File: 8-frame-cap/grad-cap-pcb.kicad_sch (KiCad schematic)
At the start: 15 parts, among them J1 B02B-XASK-1LFSN, SW1 CUS-13TB, U1 MC74HC73ADR2G, U2 SN74HCS238DYYR, U3 ICM7555xB

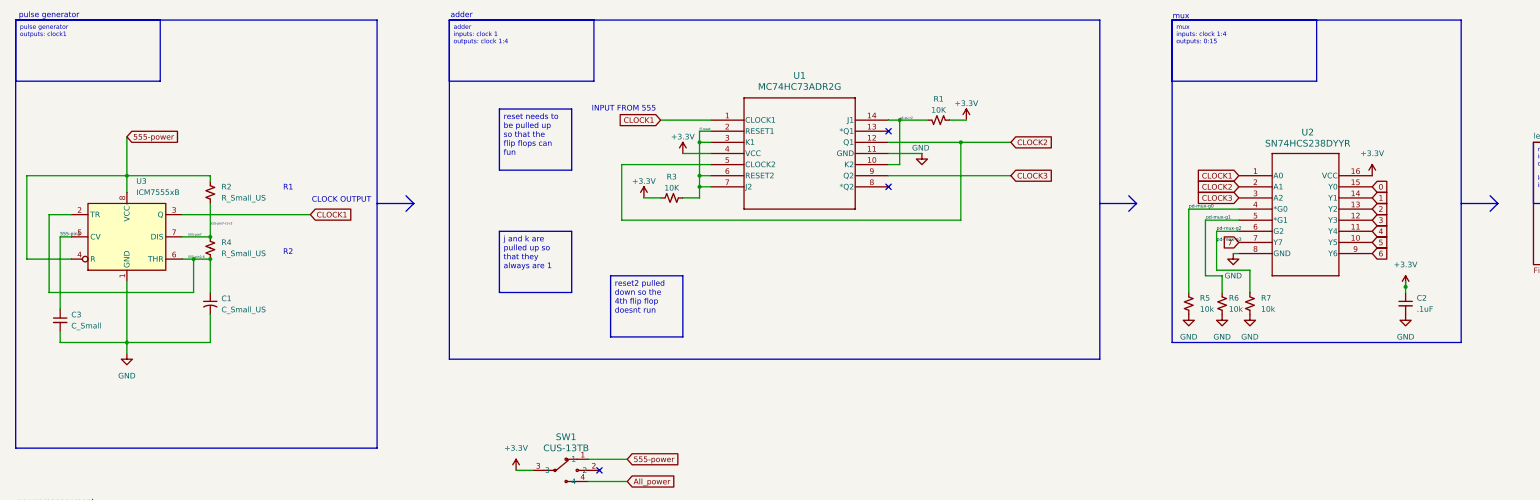
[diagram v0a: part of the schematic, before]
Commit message: routed traces, reorganized, renamed
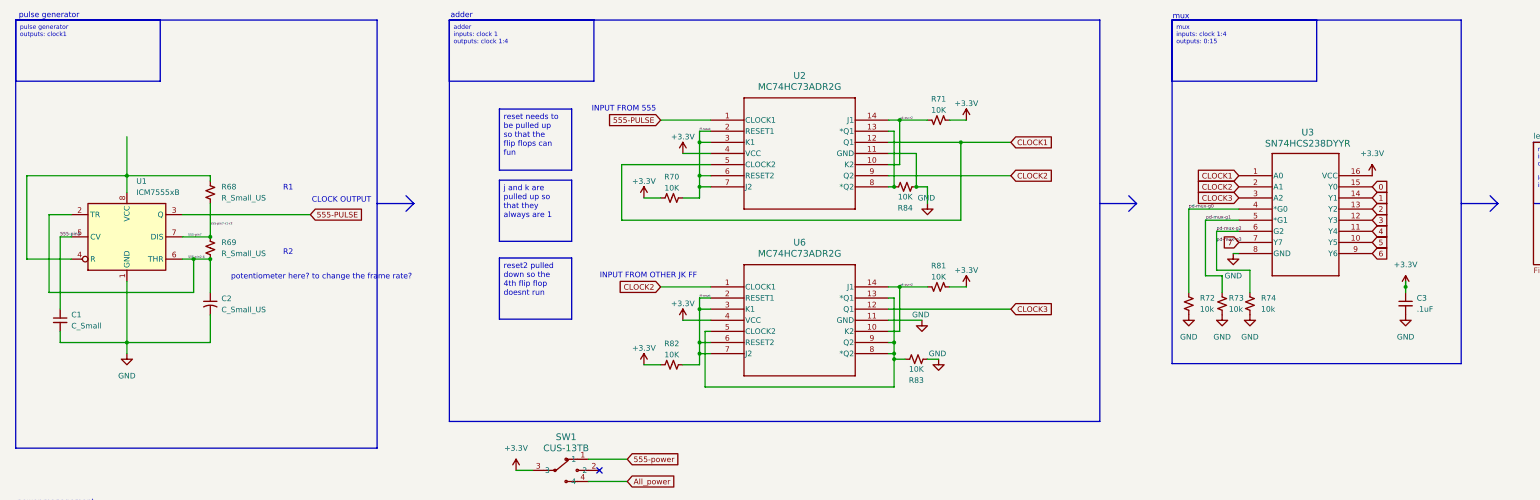
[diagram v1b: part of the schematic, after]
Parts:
- added R81, R82, R83, R84: 10K, Capacitor_SMD:C_0402_1005Metric_Pad0.74x0.62mm_HandSolder, symbol Device:R_Small_US
- added U6: MC74HC73ADR2G, GRAD-CAP:MC74HC73ADR2G_JK-FLIPFLOP, symbol MC74HC73ADR2G_JK-FLIPFLOP:MC74HC73ADR2G
- C1: renamed from C3; footprint Capacitor_SMD:C_0805_2012Metric_Pad1.18x1.45mm_HandSolder -> Capacitor_SMD:C_0603_1608Metric_Pad1.08x0.95mm_HandSolder
- C2: renamed from C1; footprint Capacitor_SMD:C_0805_2012Metric_Pad1.18x1.45mm_HandSolder -> Capacitor_SMD:C_0603_1608Metric_Pad1.08x0.95mm_HandSolder
- C3: renamed from C2; footprint Capacitor_SMD:C_0805_2012Metric_Pad1.18x1.45mm_HandSolder -> Capacitor_SMD:C_0603_1608Metric_Pad1.08x0.95mm_HandSolder
- R68: renamed from R2; footprint Resistor_SMD:R_0805_2012Metric_Pad1.20x1.40mm_HandSolder -> Resistor_SMD:R_0603_1608Metric_Pad0.98x0.95mm_HandSolder
- R69: renamed from R4; footprint Resistor_SMD:R_0805_2012Metric_Pad1.20x1.40mm_HandSolder -> Resistor_SMD:R_0603_1608Metric_Pad0.98x0.95mm_HandSolder
- R70: renamed from R3; footprint Resistor_SMD:R_0805_2012Metric_Pad1.20x1.40mm_HandSolder -> Capacitor_SMD:C_0402_1005Metric_Pad0.74x0.62mm_HandSolder
- R71: renamed from R1; footprint Resistor_SMD:R_0805_2012Metric_Pad1.20x1.40mm_HandSolder -> Capacitor_SMD:C_0402_1005Metric_Pad0.74x0.62mm_HandSolder
- R72: renamed from R5; footprint Capacitor_SMD:C_0805_2012Metric_Pad1.18x1.45mm_HandSolder -> Capacitor_SMD:C_0402_1005Metric_Pad0.74x0.62mm_HandSolder
- R73: renamed from R6; footprint Capacitor_SMD:C_0805_2012Metric_Pad1.18x1.45mm_HandSolder -> Capacitor_SMD:C_0402_1005Metric_Pad0.74x0.62mm_HandSolder
- R74: renamed from R7; footprint Capacitor_SMD:C_0805_2012Metric_Pad1.18x1.45mm_HandSolder -> Capacitor_SMD:C_0402_1005Metric_Pad0.74x0.62mm_HandSolder
- SW1: now left out of the parts list
- renumbered U3 to U1, U1 to U2, U2 to U3
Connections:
- net +3.3V: now also R81.1, R82.1, U6.4 (VCC)
- net 555-power: no longer R68.1, U1.4 (R), U1.8 (VCC)
- net CLOCK1: now also U2.12 (Q1), U2.5 (CLOCK2); no longer U1.3 (Q), U2.1 (CLOCK1)
- net CLOCK2: now also U2.9 (Q2), U6.1 (CLOCK1); no longer U2.12 (Q1), U2.5 (CLOCK2)
- net CLOCK3: now also U6.12 (Q1); no longer U2.9 (Q2)
- net GND: now also R83.1, R84.1, U6.11 (GND)
- net ff-reset: now also R82.2, U6.2 (RESET1), U6.3 (K1), U6.6 (RESET2), U6.7 (J2)
- net u4-pu-r2: now also R81.2, U6.10 (K2), U6.14 (J1)
- net at U2.13 (*Q1): now also U2.8 (*Q2), R84.2
- new net: R83.2, U6.13 (*Q1), U6.5 (CLOCK2), U6.8 (*Q2), U6.9 (Q2)
- new net: R68.1, U1.4 (R), U1.8 (VCC)
- new net 555-PULSE: U1.3 (Q), U2.1 (CLOCK1)
- no-connect marks 3 -> 1
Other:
- note added: "INPUT FROM OTHER JK FF"
- note added: "potentiometer here? to change the frame rate?"

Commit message: updated pcb
error checking
90* angles removal
schematic relinking
reorganizing schematic
fixed footprints for PHPT6 (mosfets, they didnt like the pads and the body being "different" pours or something)
silkscreen reorg
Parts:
- removed C2: C_Small_US, Capacitor_SMD:C_0603_1608Metric_Pad1.08x0.95mm_HandSolder, symbol Device:C_Small_US
- removed U1: ICM7555xB, Package_SO:SOIC-8_3.9x4.9mm_P1.27mm, symbol Timer:ICM7555xB
- added C2, C4: .1uF, Capacitor_SMD:C_0603_1608Metric_Pad1.08x0.95mm_HandSolder, symbol Device:C_Small
- added R75, R76, R77: 10k, Resistor_SMD:R_0603_1608Metric_Pad0.98x0.95mm_HandSolder, symbol Device:R_Small_US
- added T1, T2, T3, T4, T5, T6, T7: PHPT610035PKX, GRAD-CAP:PHPT610035PKX_TRANS-2PNP-100V-3A, symbol PHPT610035PKX_TRANS-2PNP-100V-3A:PHPT610035PKX
- added U1: MIC1557YM5-TR, SOT-23-5_M5_MCH, symbol MIC1557:MIC1557YM5-TR
- added U4, U5: SN74AHCT32DBR, GRAD-CAP:SN74AHCT32DBR_2-INPUT-QUAD-OR, symbol SN74AHCT32DBR_2-INPUT-QUAD-OR:SN74AHCT32DBR
- C1: value C_Small -> .68uF
- R68: value R_Small_US -> 1M
- R69: value R_Small_US -> 270k
- R70, R71, R72, R73, R74, R81, R82, R83, R84: footprint Capacitor_SMD:C_0402_1005Metric_Pad0.74x0.62mm_HandSolder -> Resistor_SMD:R_0603_1608Metric_Pad0.98x0.95mm_HandSolder
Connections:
- net 555-pin2-6 is gone; now on net 557-PULSE: R69.2
- net +3.3V: now also R68.1, C2.1, C4.1, T1.1 (EMITTER), T1.3 (EMITTER), T2.1 (EMITTER), T2.3 (EMITTER), T3.1 (EMITTER), T3.3 (EMITTER), T4.1 (EMITTER), T4.3 (EMITTER), T5.1 (EMITTER), T5.3 (EMITTER), T6.1 (EMITTER), T6.3 (EMITTER), T7.1 (EMITTER), T7.3 (EMITTER), U1.4 (VS), U4.14 (VCC), U5.14 (VCC)
- net 0: now also U5.1 (1A), U5.12 (4A)
- net 1: now also U5.2 (1B), U5.4 (2A)
- net 2: now also U5.5 (2B)
- net 3: now also U4.9 (3A)
- net 4: now also U4.10 (3B), U4.2 (1B)
- net 5: now also U4.1 (1A), U4.13 (4B)
- net 6: now also U4.12 (4A), U5.9 (3A)
- net 7: now also U5.10 (3B), U5.13 (4B)
- net GND: now also C2.2, C4.2, R75.2, R76.2, R77.2, U1.2 (GND), U4.7 (GND), U5.7 (GND)
- net 555-PULSE renamed 557-PULSE
- net 557-PULSE: now also U1.5 (OUT)
- net 555-pin5: no longer names the net of C1.1
- net 555-pin5: now also R69.1, U1.1 (T/T)
- net 555-pin7: no longer names the net of R68.2
- net 555-pin7: now also U1.3 (CS); no longer R69.1
- net ff-reset renamed ff-reset1
- net ff-reset1: no longer R82.2, U6.2 (RESET1), U6.3 (K1), U6.6 (RESET2), U6.7 (J2)
- net u4-pu-r2 renamed u4-pu-r2-1
- net u4-pu-r2-1: no longer R81.2, U6.10 (K2), U6.14 (J1)
- new net 10b: T5.4 (BASE)
- new net 10c: T5.5 (COLLECTOR), T5.6 (COLLECTOR)
- new net 11b: T6.2 (BASE)
- new net 11c: T6.7 (COLLECTOR), T6.8 (COLLECTOR)
- new net 12b: T6.4 (BASE)
- new net 12c: T6.5 (COLLECTOR), T6.6 (COLLECTOR)
- new net 13b: T7.2 (BASE)
- new net 13c: T7.8 (COLLECTOR)
- new net 14b: T7.4 (BASE)
- new net 14c: T7.6 (COLLECTOR)
- new net 1b: T1.2 (BASE)
- new net 1c: T1.7 (COLLECTOR), T1.8 (COLLECTOR)
- new net 2b: T1.4 (BASE)
- new net 2c: T1.5 (COLLECTOR), T1.6 (COLLECTOR)
- new net 3b: T2.2 (BASE)
- new net 3c: T2.7 (COLLECTOR), T2.8 (COLLECTOR)
- new net 4b: T2.4 (BASE)
- new net 4c: T2.5 (COLLECTOR), T2.6 (COLLECTOR)
- new net 5b: T3.2 (BASE)
- new net 5c: T3.7 (COLLECTOR), T3.8 (COLLECTOR)
- new net 6b: T3.4 (BASE)
- new net 6c: T3.5 (COLLECTOR), T3.6 (COLLECTOR)
- new net 7b: T4.2 (BASE)
- new net 7c: T4.7 (COLLECTOR), T4.8 (COLLECTOR)
- new net 8b: T4.4 (BASE)
- new net 8c: T4.5 (COLLECTOR), T4.6 (COLLECTOR)
- new net 9b: T5.2 (BASE)
- new net 9c: T5.7 (COLLECTOR), T5.8 (COLLECTOR)
- new net f1or2: U5.3 (1Y)
- new net f1or8: U5.11 (4Y)
- new net f2or3: U5.6 (2Y)
- new net f4or5: U4.8 (3Y)
- new net f5or6: U4.3 (1Y)
- new net f6or7: U4.11 (4Y)
- new net f7or8: U5.8 (3Y)
- new net ff-reset2: R82.2, U6.2 (RESET1), U6.3 (K1), U6.6 (RESET2), U6.7 (J2)
- new net u3-pd-3a: R76.1, U4.5 (2B)
- new net u3-pd-3b: R75.1, U4.4 (2A)
- new net u3-pd-3y: R77.1, U4.6 (2Y)
- new net u4-pu-r2-2: R81.2, U6.10 (K2), U6.14 (J1)
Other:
- note added: "2-INPUT-QUAD-OR"
- note added: "MOSFETS"
- note added: "OR GATES"
- note removed: "CLOCK OUTPUT"
- note removed: "R1"
- note removed: "R2"
- note removed: "potentiometer here? to change the frame rate?"
- note removed: "power management"
- moved on the sheet: C3, J1, R70, R71, R72, R73, R74, R81, R82, R83, R84, SW1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

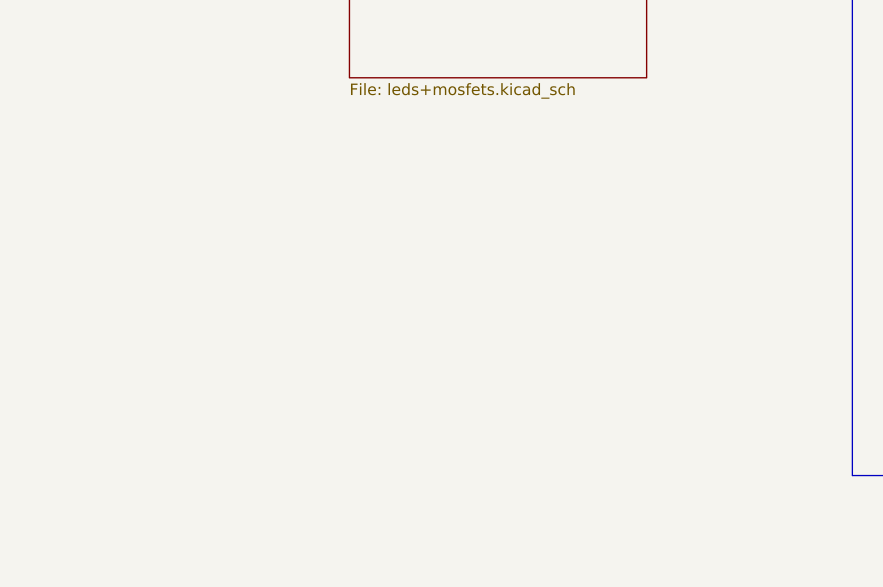
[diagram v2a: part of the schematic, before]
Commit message: updated pcb
shrunk edge cuts
moved led matrix header (again)
added 3d file links
added mounting holes
added 3 on board buttons
fixed unused pin header connections
discovered polygon filled area default chamfer (i will be using this always now)
updated bom with new caps
added status LED for usbc power in
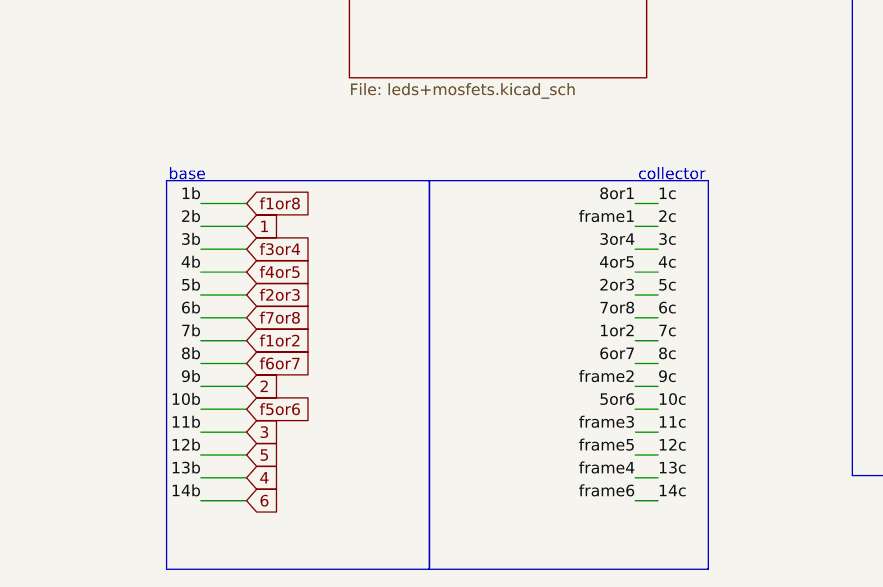
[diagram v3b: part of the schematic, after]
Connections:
- net 10b is gone; now on net f5or6: T5.4 (BASE)
- net 11b is gone; now on net 3: T6.2 (BASE)
- net 12b is gone; now on net 5: T6.4 (BASE)
- net 13b is gone; now on net 4: T7.2 (BASE)
- net 14b is gone; now on net 6: T7.4 (BASE)
- net 1b is gone; now on net f1or8: T1.2 (BASE)
- net 2b is gone; now on net 1: T1.4 (BASE)
- net 4b is gone; now on net f4or5: T2.4 (BASE)
- net 5b is gone; now on net f2or3: T3.2 (BASE)
- net 6b is gone; now on net f7or8: T3.4 (BASE)
- net 7b is gone; now on net f1or2: T4.2 (BASE)
- net 8b is gone; now on net f6or7: T4.4 (BASE)
- net 9b is gone; now on net 2: T5.2 (BASE)
- net 3b renamed f3or4
- net 5c renamed 2or3
- net 7c renamed 1or2
- net 8c renamed 6or7
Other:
- note added: "base"
- note added: "collector"

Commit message: updated from prototyping
- jk ff -> incrementer
- shrink to be cap size
- rename labels to match layout
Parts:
- removed C2, C4: .1uF, Capacitor_SMD:C_0603_1608Metric_Pad1.08x0.95mm_HandSolder, symbol Device:C_Small
- removed R70, R71, R81, R82, R83, R84: 10K, Resistor_SMD:R_0603_1608Metric_Pad0.98x0.95mm_HandSolder, symbol Device:R_Small_US
- removed U2, U6: MC74HC73ADR2G, GRAD-CAP:MC74HC73ADR2G_JK-FLIPFLOP, symbol MC74HC73ADR2G_JK-FLIPFLOP:MC74HC73ADR2G
- added U2: SN74HC163DR, GRAD-CAP:binary counter - 74hc163, symbol binary counter - 74hc163:SN74HC163DR
- C1: value .68uF -> .1uF
- R69: value 270k -> CHECK VALUE
- U1: footprint SOT-23-5_M5_MCH -> GRAD-CAP:MIC1557
- U4, U5: footprint GRAD-CAP:SN74AHCT32DBR_2-INPUT-QUAD-OR -> DB14
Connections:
- net +3.3V: now also U2.1 (*CLR), U2.10 (ENT), U2.16 (VCC), U2.7 (ENP), U2.9 (*LOAD)
- net 557-PULSE: now also U2.2 (CLK)
- net CLOCK1: now also U2.13 (QB)
- net CLOCK2: now also U2.12 (QC)
- net CLOCK3: now also U2.11 (QD)
- net GND: now also U2.3 (A), U2.4 (B), U2.5 (C), U2.6 (D), U2.8 (GND)
- net 10c renamed 5or6
- net 11c renamed frame3
- net 12c renamed frame5
- net 13c renamed frame4
- net 14c renamed frame6
- net 1c renamed 8or1
- net 2c renamed frame1
- net 3c renamed 3or4
- net 4c renamed 4or5
- net 6c renamed 7or8
- net 9c renamed frame2
- no-connect marks 1 -> 3
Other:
- sheet leds+mosfets renamed LEDs
- note removed: "INPUT FROM 555"
- note removed: "INPUT FROM OTHER JK FF"
- company: (none) -> Julia Laine
- title: (none) -> Main-Sheet
- moved on the sheet: C3, J1, R72, R73, R74, R75, R76, R77, SW1, T1, T2, T3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

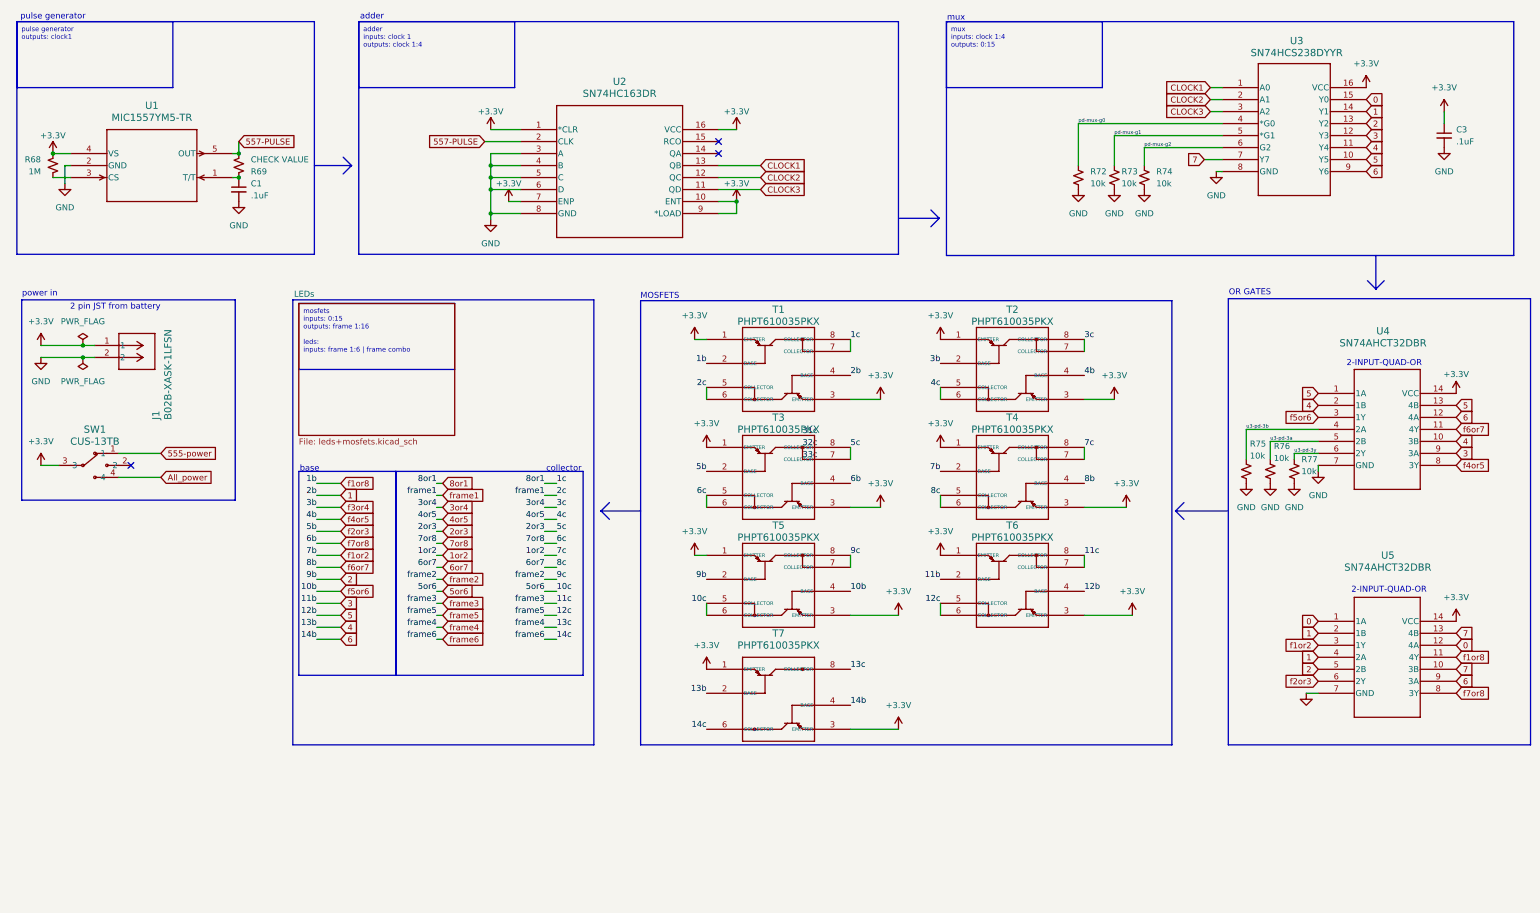
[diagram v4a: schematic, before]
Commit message: updated pcb
added labels for each diode
changed silkscreen to be handwriting
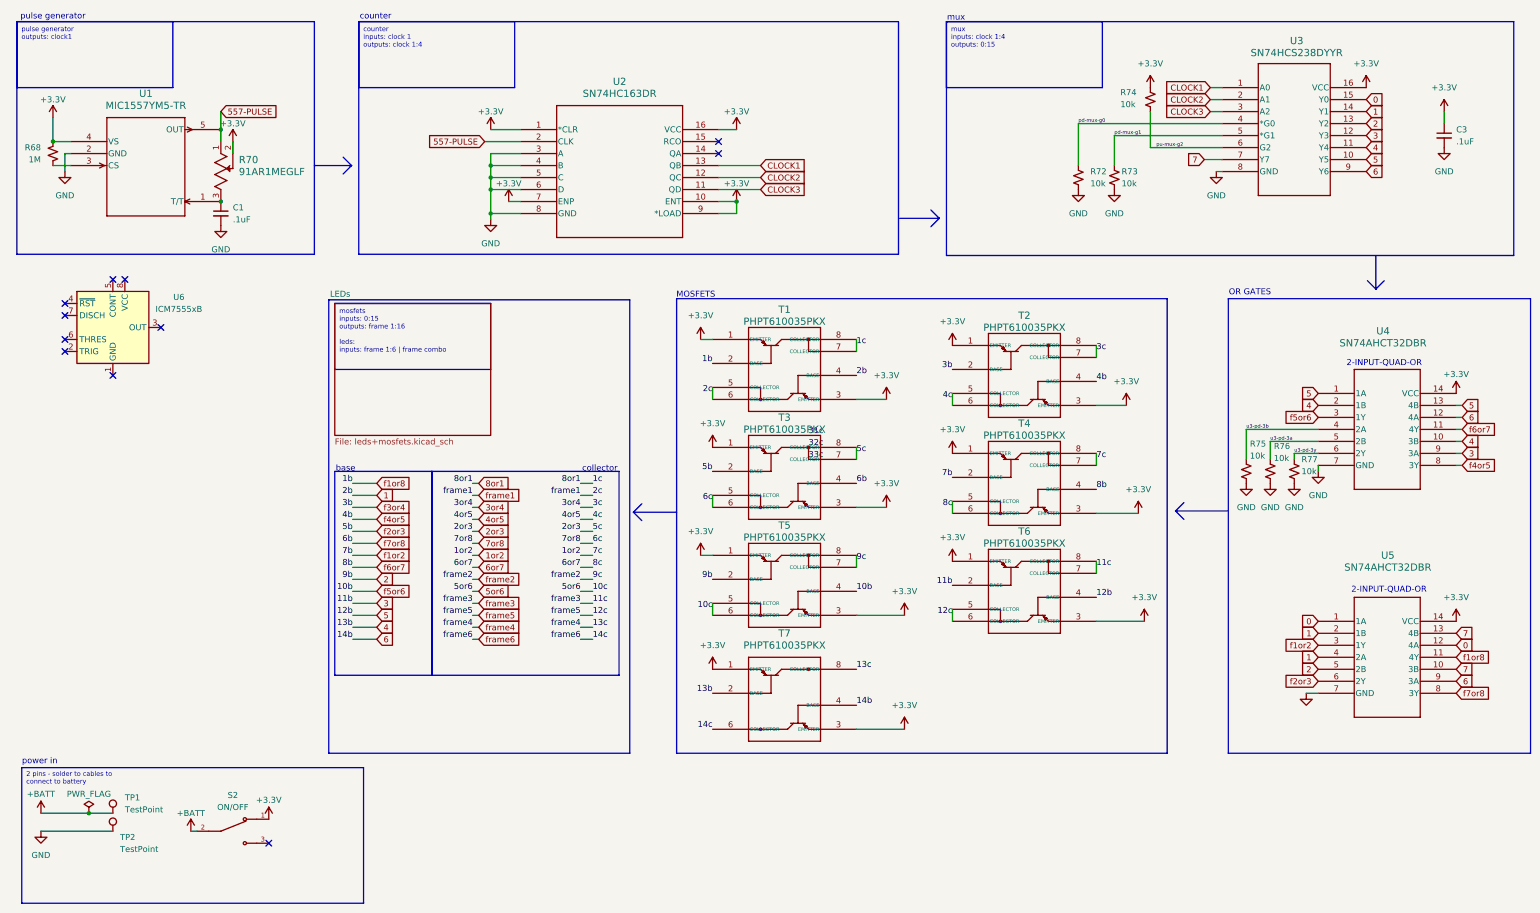
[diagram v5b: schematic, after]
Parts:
- removed J1: B02B-XASK-1LFSN, GRAD-CAP:1X02JST, symbol 1X02_JST:B02B-XASK-1LFSN
- removed R69: CHECK VALUE, Resistor_SMD:R_0603_1608Metric_Pad0.98x0.95mm_HandSolder, symbol Device:R_Small_US
- removed SW1: CUS-13TB, CUS-13TB_NDC, symbol sp3t-slide-switch:CUS-13TB
- added R70: 91AR1MEGLF, GRAD-CAP:1M-potentiometer, symbol 1M-potentiometer:91AR1MEGLF
- added S2: ON/OFF, GRAD-CAP:spdt-switch, symbol spdt-switch:EG1215AA
- added TP1: TestPoint, TestPoint:TestPoint_THTPad_D2.5mm_Drill1.2mm, symbol testpoint:TestPoint
- added TP2: TestPoint, Connector_PinHeader_2.54mm:PinHeader_1x01_P2.54mm_Vertical, symbol testpoint:TestPoint
- added U6: ICM7555xB, Package_SO:SOIC-8_3.9x4.9mm_P1.27mm, symbol Timer:ICM7555xB
- U1: footprint GRAD-CAP:MIC1557 -> SOT-23-5_M5_MCH
- U2: footprint GRAD-CAP:binary counter - 74hc163 -> kicad_library:74hc163dr
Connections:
- net +3.3V: now also R74.2, R70.2, S2.1
- net 557-PULSE: now also R70.1
- net GND: now also TP2.1; no longer R74.2
- net at C1.1, U1.1 (T/T): now also R70.3
- net pd-mux-g2 renamed pu-mux-g2
- new net +BATT: S2.2, TP1.1
- no-connect marks 3 -> 11
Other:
- note added: "counter"
- note removed: "2 pin JST from battery"
- note removed: "adder"
- moved on the sheet: C1, R68, R74, T1, T2, T3, T4, T5, T6, T7, U1
